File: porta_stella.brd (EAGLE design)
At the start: 220 x 100 mm, 80 parts, among them IC1 74LS00D, T1 2N3904, T2 PN3906, T3 PN3906, T4 PN3906, X1 SSW-112-02-G-Q

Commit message: Started work on controller daughterboard
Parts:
- removed C12: 1F, resistor:E3,5-8
- removed C13: 100nF, resistor:C0805
- removed ON/OFF: ON/OFF, special:EDG-01
- removed PAD1: AUD, wirepad:4,16O1,6
- removed PAD2: CVID, wirepad:4,16O1,6
- removed SV1: (no value), con-lstb:MA03-1
- removed USB1: ZX62-B-5PA, Seeed-Connector:MICRO-USB5+6P-SMD-0.65-AB
- added AUD: AUD, wirepad:2,54/1,1
- added C22: 10uf, adafruit:C0805
- added C5: 10uF, resistor:C1210
- added C6: 2.2uF, adafruit:C0805
- added C7: 0.1uF, adafruit:C0805
- added CHRG/LBO: ORANGE, piboy_new:ADAFRUIT_CHIPLED_0603
- added CN4: MicroUSB, microbuilder:4UCONN_20329
- added CVID: CVID, wirepad:2,54/1,1
- added DONE: GREEN, piboy_new:ADAFRUIT_CHIPLED_0603
- added GND_A: GND_A, wirepad:2,54/1,1
- added GND_V: GND_V, wirepad:2,54/1,1
- added L1: 6.8uH, microbuilder:INDUCTOR_5X5MM_TDK_VLC5045
- added LBO: RED, piboy_new:ADAFRUIT_CHIPLED_0603
- added ON: BLUE, piboy_new:ADAFRUIT_CHIPLED_0603
- added ON/OFF1: ON/OFF, special:EDG-01
- added R13, R36, R44, R45: 1K, adafruit:R0805
- added R37, R39: 200K, adafruit:R0805
- added R38, R41: 1.87M, adafruit:R0805
- added R40: 340K, adafruit:R0805
- added R42: 270K, adafruit:R0805
- added R43, R47: 100K, adafruit:R0805
- added R46: 1.0K, adafruit:R0805
- added SV2: (no value), con-lstb:MA10-1
- added T5: MMUN2133LT1G, piboy_new:TRANSISTOR_SC59-BEC
- added THERM: 15K, adafruit:R0805
- added U1: TPS61090RSAR, microbuilder:PVQFN-16
- added U2: MCP73871, microbuilder:QFN20_4MM
- C21: value 100nF -> 10uF; device resistor:C0805 -> resistor:C1210
- C9: value 68nF -> 10uF; device resistor:C0805 -> resistor:C1210
- S3, S4: device SparkFun-Switches:TACTILE_SWITCH_PTH_6.0MM_KIT -> SparkFun-Switches:TACTILE_SWITCH_SMD_6.0X3.5MM
- moved S4 134.0 mm to (162.1, 22.0), turned to 0 degrees
- moved C8 123.6 mm to (157.8, 9.83)
- moved C10 113.3 mm to (170.2, 39.2)
- moved C17 113.3 mm to (144.6, 85.6), turned to 0 degrees
- moved C9 111.8 mm to (14.0, -32.0), flipped to the top, turned to 0 degrees
- moved R34 111.5 mm to (141.1, 9.75), turned to 270 degrees
- moved C21 102.3 mm to (20.0, -32.0), flipped to the top, turned to 0 degrees
- moved JP1 102.1 mm to (168.1, 32.4), flipped to the bottom
- moved S3 97.5 mm to (136.5, 21.8), turned to 0 degrees
- moved C14 96.2 mm to (138.0, 59.5)
- moved LDIFF 87.2 mm to (125.0, 93.5), turned to 180 degrees
- moved PAUSE 86.4 mm to (171.0, 93.5), turned to 0 degrees
- moved COLOR 50.1 mm to (136.6, 74.6), turned to 180 degrees
- moved R33 26.6 mm to (170.1, 43.5), turned to 270 degrees
- moved C16 10.1 mm to (149.1, 36.3), turned to 90 degrees
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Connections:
- new net BOOST_ENABLE: ON/OFF1.1, R37.2, U1.11
- new net LBO: T5.B, U1.12
- new net N$10: L1.P$2, U1.3, U1.4
- new net N$12: R40.2, R41.1, U1.9
- new net N$22: LBO.A, R13.1
- new net N$37: R38.1, R39.2, U1.14
- new net N$41: R13.2, T5.C
- new net N$42: ON.A, R36.2
- new net N$43: R42.1, R43.1, U2.P$2
- new net N$44: R45.1, U2.P$7
- new net N$45: R44.1, U2.P$8
- new net N$46: R46.2, U2.P$13
- new net N$47: THERM.2, U2.P$5
- new net N$48: DONE.C, R45.2
- new net N$49: CHRG/LBO.C, R44.2
- new net N$50: R47.2, U2.P$12
- new net VBAT: C5.1, C7.1, L1.P$1, R37.1, R41.2, T5.E, U1.8, U2.P$1, U2.P$20
- new net VLIPO: C21.1, U2.P$14, U2.P$15, U2.P$16
- net +5V: now also C6.1, C9.1, R36.1, R38.2, SV3.2, U1.1, U1.15, U1.16; no longer C12.+, C13.1, ON/OFF.2
- net GND: now also C22.2, C5.2, C6.2, C7.2, CN4.BASE@1, CN4.BASE@2, CN4.D+, CN4.D-, CN4.GND, CN4.ID, CN4.SPRT@1, CN4.SPRT@2, CN4.SPRT@3, CN4.SPRT@4, GND_A.1, GND_V.1, LBO.C, ON.C, ON/OFF1.2, R39.1, R40.1, R43.2, R46.1, R47.1, S3.2, S4.2, SV2.1, THERM.1, U1.10, U1.13, U1.5, U1.6, U1.7, U1.P$18, U1.P$19, U1.P$20, U1.P$21, U1.P$22, U1.THERMAL, U2.P$10, U2.P$11, U2.P$21; no longer C12.-, C13.2, S3.3, S4.3, SV1.2, SV1.3, USB1.2, USB1.3, USB1.4, USB1.5, USB1.P1, USB1.P2, USB1.P3, USB1.P4, USB1.P5, USB1.P6
- net LFT_FIRE: now also SV2.4
- net LFT_JOY_DWN: now also SV2.9
- net LFT_JOY_LFT: now also SV2.8
- net LFT_JOY_RGT: now also SV2.7
- net LFT_JOY_UP: now also SV2.10
- net LFT_PADDLE_A: now also SV2.6
- net LFT_PADDLE_B: now also SV2.5; no longer C9.1
- net N$25: now also CVID.1; no longer PAD2.1
- net N$28: now also AUD.1; no longer PAD1.1
- net P_SW: now also SV2.3
- net VBUS: now also C22.1, CHRG/LBO.A, CN4.VBUS, DONE.A, R42.2, U2.P$17, U2.P$18, U2.P$19, U2.P$3, U2.P$4, U2.P$9; no longer ON/OFF.1, SV1.1, USB1.1
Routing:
- net D1: track 75.6 -> 68.8 mm
- net D8: track 134.6 -> 136.6 mm, vias 6 -> 5
- net A8: track 18.6 -> 19.9 mm
- net A5: track 50.9 -> 52.1 mm
- net A6: track 54.8 -> 56.1 mm
- net D7: track 129.7 -> 130.7 mm, vias 4 -> 3
- net A4: track 49.3 -> 50.2 mm
- net A3: track 48.0 -> 48.9 mm
- net D6: track 107.8 -> 108.6 mm
- net A11: track 25.4 -> 26.2 mm
- net A10: track 23.1 -> 23.7 mm
- net A9: track 57.9 -> 57.3 mm, vias 3 -> 2
- net A2: track 48.2 -> 48.8 mm
- removed copper zone on layer 1, net GND
- removed copper zone on layer 16, net GND
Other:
- board size 220 x 100 mm -> 52 x 99 mm
- board text removed: "+5V"
- board text removed: "A0"
- board text removed: "A1"
- board text removed: "A10"
- board text removed: "A11"
- board text removed: "A12"
- board text removed: "A2"
- board text removed: "A3"
- board text removed: "A4"
- board text removed: "A5"
- board text removed: "A6"
- board text removed: "A7"
- board text removed: "A8"
- board text removed: "A9"
- board text removed: "ADDRESS BUS"
- board text removed: "AU1"
- board text removed: "AU2"
- board text removed: "AUDIO"
- board text removed: "Atari Television Interface Adapter"
- board text removed: "B/W"
- board text removed: "BLK"
- board text removed: "BUTTONS"
- board text removed: "BW/ COLOR"
- board text removed: "CLK"
- board text removed: "COL"
- board text removed: "CS1"
- board text removed: "D1"
- board text removed: "D2"
- board text removed: "D3"
- board text removed: "D4"
- board text removed: "D5"
- board text removed: "D6"
- board text removed: "D7"
- board text removed: "D8"
- board text removed: "DATA BUS"
- board text removed: "DEL"
- board text removed: "DWN"
- board text removed: "GND"
- board text removed: "IRQ"
- board text removed: "LEFT DIFF."
- board text removed: "LEFT FIRE"
- board text removed: "LEFT JOYSTICK"
- board text removed: "LEFT PADDLE A"
- board text removed: "LEFT PADDLE B"
- board text removed: "LEFT PLAYER"
- board text removed: "LFT"
- board text removed: "LM0"
- board text removed: "LM1"
- board text removed: "LM2"
- board text removed: "MOS Technologies 6507 Microprocessor"
- board text removed: "MOS Technologies 6532 RIOT Chip"
- board text removed: "PADDLES"
- board text removed: "PB2"
- board text removed: "PB4"
- board text removed: "PB5"
- board text removed: "PHI0"
- board text removed: "PHI2"
- board text removed: "R/W"
- board text removed: "RDY"
- board text removed: "RES"
- board text removed: "RESET"
- board text removed: "RGT"
- board text removed: "RIGHT DIFF."
- board text removed: "RIGHT FIRE"
- board text removed: "RIGHT JOYSTICK"
- board text removed: "RIGHT PADDLE A"
- board text removed: "RIGHT PADDLE B"
- board text removed: "RIGHT PLAYER"
- board text removed: "SELECT"
- board text removed: "START"
- board text removed: "SWITCHES"
- board text removed: "SYNC"
- board text removed: "This chip serves two functions; It holds the system's 128 bytes of RAM and gives the CPU more I/O so it can connect with all the controllers and difficulty switches."
- board text removed: "This chip was custom manufactured by Atari and is responsible for drawing everything on the screen, producing sound, and reading some controller input. It's considered by many to be the soul of the system"
- board text removed: "This was a cost reduced version of the very popular 6502 processor"
- board text removed: "UP"
- board text removed: "Use at least 500mA Supply"
- board text removed: "VIDEO"

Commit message: reworked the shape
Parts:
- removed SV2, SV3: (no value), con-lstb:MA10-1
- added J1: PJ-393, Seeed-Connector:AUDIO8P-SMD-3.5-14.5X6.1X4.0MM
- moved PAUSE 176.9 mm to (4.00, 35.0), turned to 180 degrees
- moved R40 165.2 mm to (133.1, 53.3), flipped to the bottom, turned to 180 degrees
- moved R36 161.6 mm to (132.9, 41.3), flipped to the bottom, turned to 180 degrees
- moved R38 161.4 mm to (127.4, 60.3), flipped to the bottom, turned to 90 degrees
- moved R41 159.0 mm to (133.8, 57.2), flipped to the bottom, turned to 90 degrees
- moved S4 157.3 mm to (6.00, 42.0), turned to 180 degrees
- moved S2 156.2 mm to (7.00, 24.8), turned to 90 degrees
- moved U1 154.5 mm to (128.6, 55.5), flipped to the bottom, turned to 270 degrees
- moved R44 153.0 mm to (128.8, 39.3), flipped to the bottom
- moved R45 152.3 mm to (132.9, 39.3), flipped to the bottom, turned to 180 degrees
- moved C6 152.2 mm to (129.5, 60.3), flipped to the bottom, turned to 270 degrees
- moved C9 148.1 mm to (126.9, 63.8), flipped to the bottom
- moved C5 146.4 mm to (129.1, 50.2), flipped to the bottom, turned to 270 degrees
- moved C17 143.8 mm to (15.4, 22.5), turned to 270 degrees
- moved T5 141.0 mm to (129.1, 44.2), flipped to the bottom, turned to 180 degrees
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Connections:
- net +5V: no longer SV3.2
- net GND: no longer SV2.1, SV3.1
- net LFT_FIRE: no longer SV2.4, SV3.4
- net LFT_JOY_DWN: no longer SV2.9, SV3.9
- net LFT_JOY_LFT: no longer SV2.8, SV3.8
- net LFT_JOY_RGT: no longer SV2.7, SV3.7
- net LFT_JOY_UP: no longer SV2.10, SV3.10
- net LFT_PADDLE_A: no longer SV2.6, SV3.6
- net LFT_PADDLE_B: no longer SV2.5, SV3.5
- net P_SW: no longer SV2.3, SV3.3
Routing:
- net D8: track 136.6 -> 69.5 mm, vias 5 -> 4
- net D7: track 130.7 -> 69.9 mm, vias 3 -> 2
- net A9: track 57.3 -> 0.00 mm, vias 2 -> 0
- net D6: track 108.6 -> 52.4 mm, vias 4 -> 2
- net A6: track 56.1 -> 3.52 mm, vias 1 -> 0
- net D5: track 94.9 -> 43.8 mm, vias 4 -> 2
- net D4: track 89.2 -> 41.2 mm
- net D3: track 73.9 -> 33.8 mm
- net D2: track 70.0 -> 31.7 mm
- net D1: track 68.8 -> 31.7 mm
- net A5: track 52.1 -> 22.2 mm, vias 1 -> 0
- net A4: track 50.2 -> 22.8 mm, vias 1 -> 0
- net A11: track 26.2 -> 0.00 mm, vias 1 -> 0
- net A3: track 48.9 -> 23.5 mm, vias 1 -> 0
- net A12: track 59.1 -> 34.5 mm
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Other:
- board size 52 x 99 mm -> 98 x 62 mm
- board text added: "QUARTER DOLLAR"
- board text added: "UNITED STATES OF AMERICA"

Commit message: more trace work
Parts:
- moved C6 60.1 mm to (76.2, 32.4), turned to 0 degrees
- moved C9 58.7 mm to (75.7, 34.9)
- moved L1 58.6 mm to (74.0, 37.5), turned to 0 degrees
- moved R40 58.3 mm to (75.7, 42.8), turned to 270 degrees
- moved R41 57.1 mm to (78.8, 41.9), turned to 180 degrees
- moved R38 54.5 mm to (81.2, 31.4), turned to 270 degrees
- moved R39 52.0 mm to (80.2, 34.4), turned to 180 degrees
- moved U1 51.8 mm to (79.8, 38.2), turned to 180 degrees
- moved T5 46.5 mm to (83.9, 33.4)
- moved C5 45.3 mm to (85.2, 39.0), turned to 180 degrees
- moved R37 43.9 mm to (84.7, 36.4), turned to 0 degrees
- moved ON 43.6 mm to (90.9, 29.9), turned to 270 degrees
- moved R36 43.5 mm to (90.9, 29.9), turned to 0 degrees
- moved DONE 42.8 mm to (90.8, 31.9), turned to 90 degrees
- moved R45 42.6 mm to (90.9, 31.9), turned to 0 degrees
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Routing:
- net +5V: track 0.00 -> 128.7 mm, vias 0 -> 7
- net P_SW: track 0.00 -> 30.0 mm, vias 0 -> 2
- net N$40: track 0.00 -> 28.8 mm, vias 0 -> 2
- net N$45: track 0.00 -> 28.6 mm, vias 0 -> 2
- net VBAT: track 0.00 -> 27.2 mm, vias 0 -> 1
- net VBUS: track 0.00 -> 26.3 mm, vias 0 -> 3
- net N$28: track 0.00 -> 24.5 mm, vias 0 -> 1
- net N$44: track 0.00 -> 23.8 mm, vias 0 -> 2
- net LFT_PADDLE_A: track 0.00 -> 22.6 mm
- net N$32: track 0.00 -> 22.0 mm, vias 0 -> 2
- net CPU_RDY: track 0.00 -> 21.6 mm, vias 0 -> 2
- net N$17: track 0.00 -> 20.9 mm, vias 0 -> 1
- net TIA_RDY: track 0.00 -> 17.9 mm, vias 0 -> 1
- net N$5: track 0.00 -> 17.0 mm
- net N$4: track 0.00 -> 16.5 mm, vias 0 -> 2
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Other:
- outline, holes or cut-outs redrawn

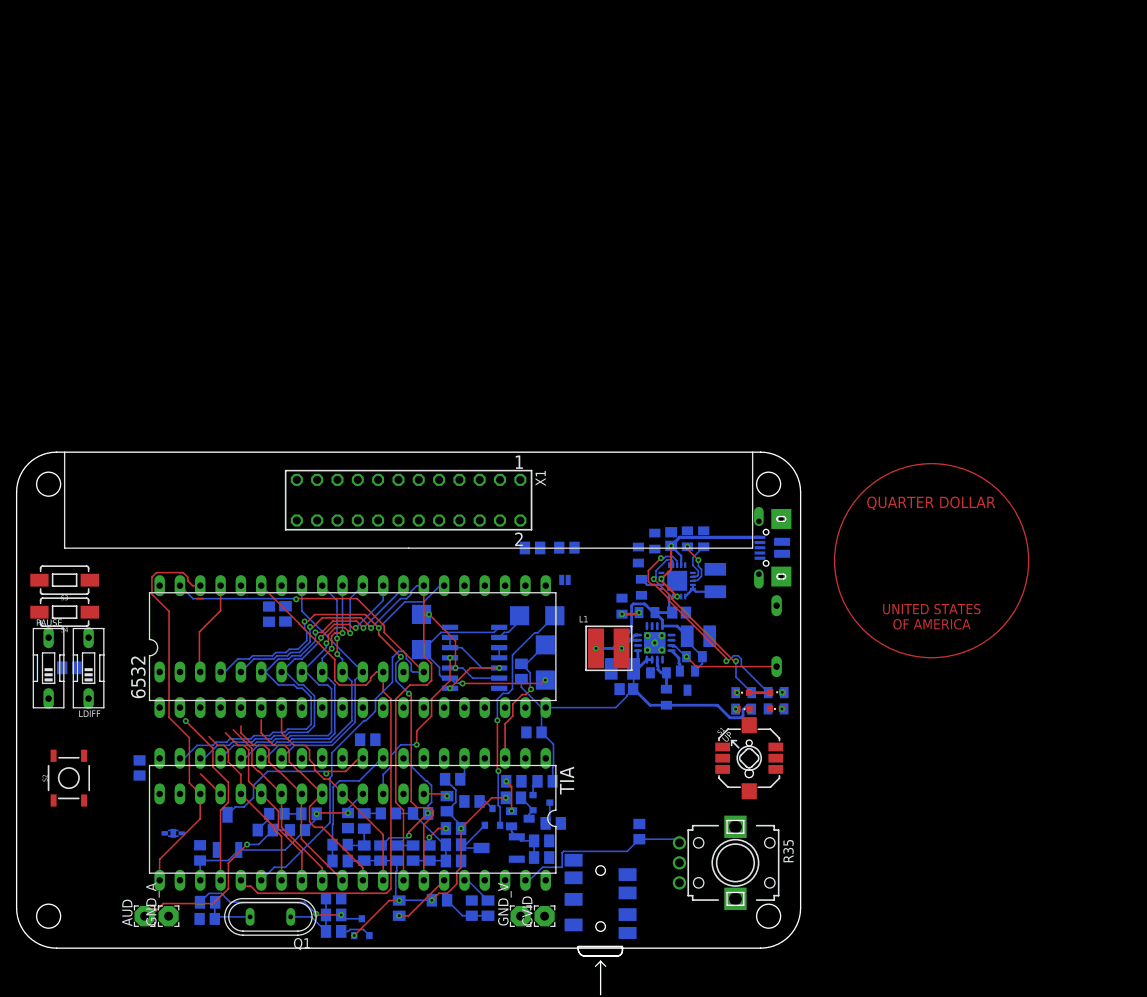
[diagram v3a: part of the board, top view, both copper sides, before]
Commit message: included measurements of the screen
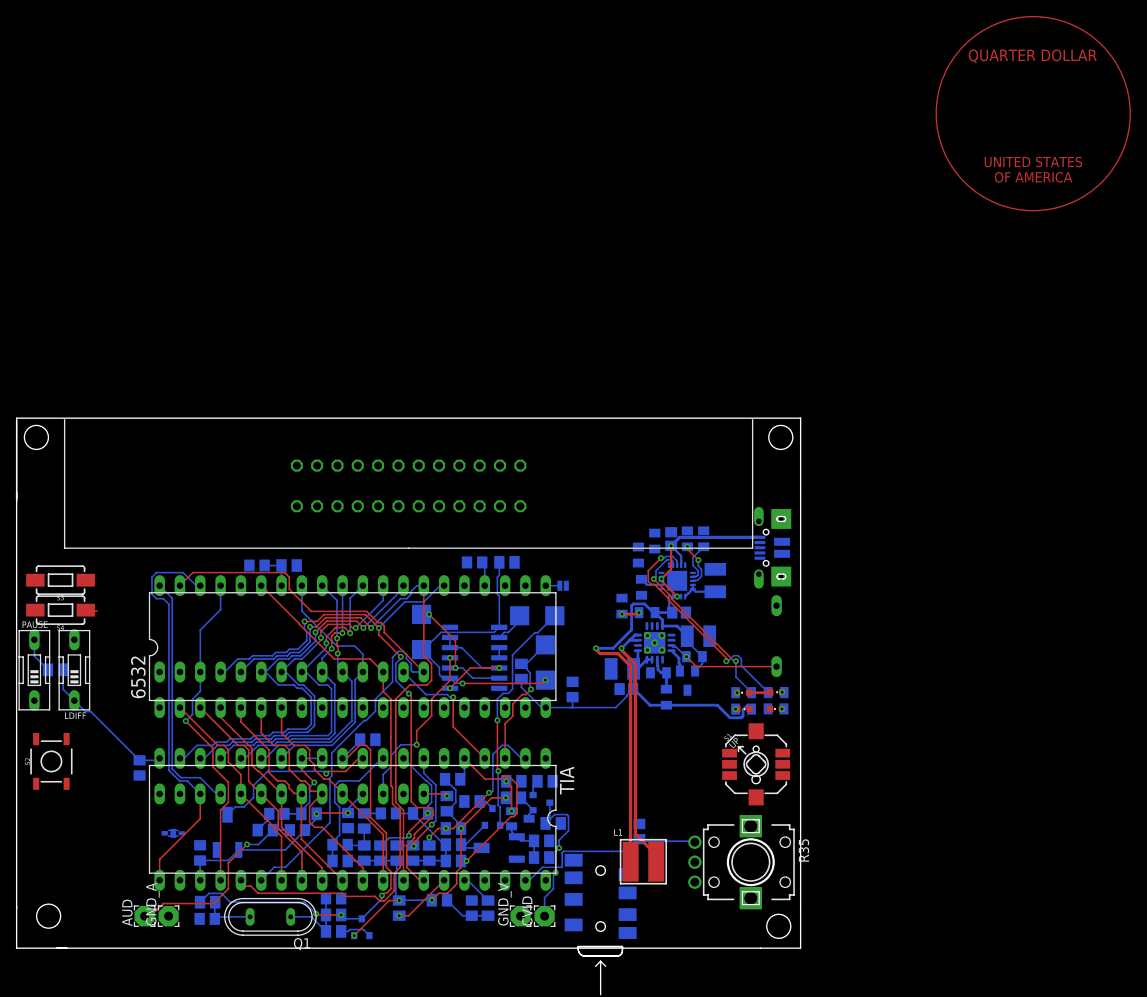
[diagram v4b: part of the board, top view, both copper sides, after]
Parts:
- moved L1 27.0 mm to (78.3, 10.8)
- moved C10 11.7 mm to (57.3, 48.2), turned to 0 degrees
- moved C16 7.21 mm to (69.5, 32.3), turned to 90 degrees
- moved C18 6.25 mm to (30.0, 47.8), turned to 0 degrees
- moved R27 6.06 mm to (34.1, 47.8), turned to 0 degrees
- moved R33 3.67 mm to (61.3, 48.2)
- moved S2 3.02 mm to (4.35, 23.3)
- moved R35 1.93 mm to (91.8, 10.7)
- moved PAUSE 1.80 mm to (2.22, 34.7)
- moved LDIFF 1.80 mm to (7.22, 34.7)
- moved R34 1.80 mm to (4.87, 34.8)
- moved X1 1.78 mm to (49.0, 57.8), flipped to the bottom
- moved S1 1.15 mm to (92.4, 23.0)
- moved JP1 0.75 mm to (68.3, 45.3), turned to 180 degrees
- moved S4 0.57 mm to (5.49, 42.3)
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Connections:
- net LFT_FIRE: now also S2.1
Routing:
- net N$32: track 22.0 -> 53.5 mm, vias 2 -> 3
- net VBAT: track 27.2 -> 56.9 mm
- net N$10: track 3.75 -> 32.2 mm
- net A6: track 3.52 -> 30.9 mm
- net N$2: track 2.83 -> 24.2 mm, vias 0 -> 1
- net N$1: track 3.54 -> 21.1 mm, vias 2 -> 3
- net N$25: track 2.81 -> 20.0 mm, vias 0 -> 2
- net PHI_0: track 0.00 -> 16.8 mm, vias 0 -> 1
- net N$3: track 2.03 -> 15.0 mm, vias 0 -> 2
- net N$27: track 2.11 -> 12.9 mm, vias 0 -> 1
- net +5V: track 128.7 -> 138.4 mm
- net N$40: track 28.8 -> 37.1 mm
- net A12: track 34.5 -> 41.3 mm
- net A5: track 22.2 -> 27.3 mm
- net N$29: track 0.00 -> 4.63 mm
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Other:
- board size 98 x 62 mm -> 98 x 66.2 mm
- board text added: "screen"

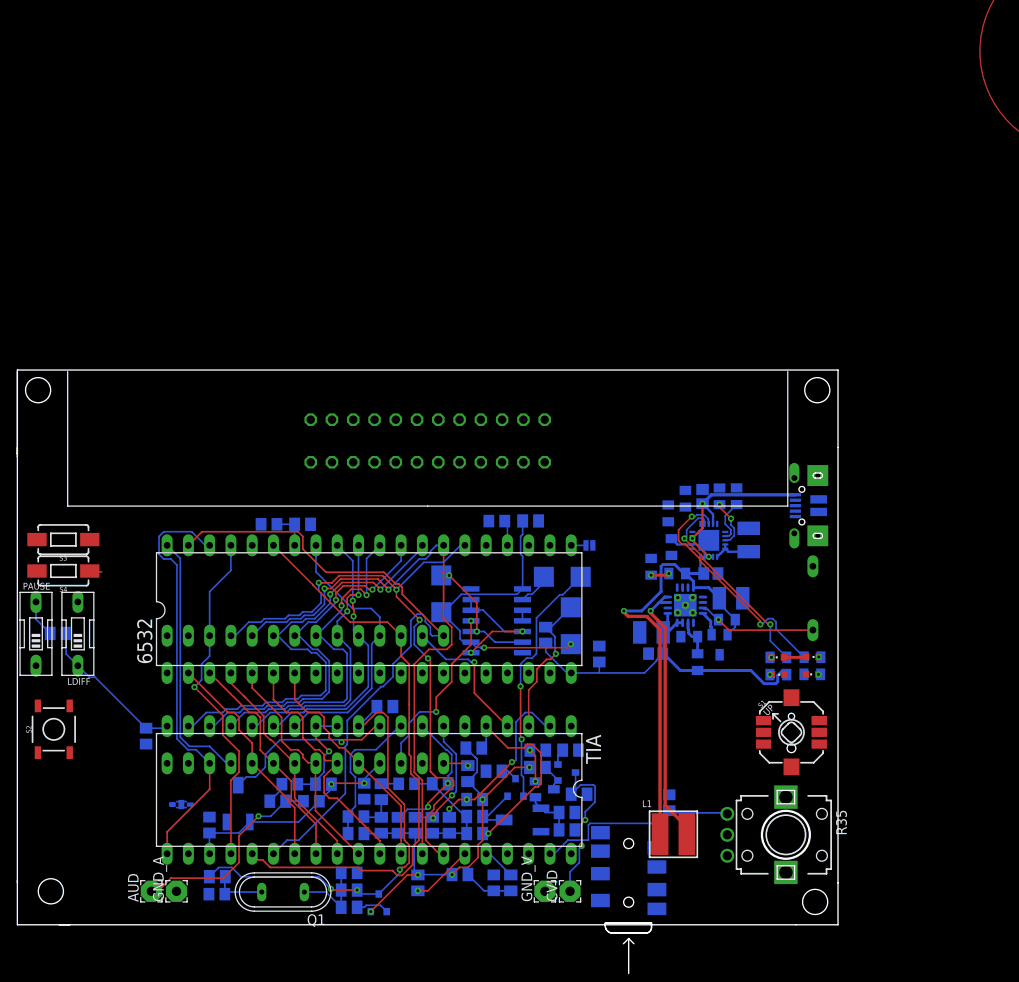
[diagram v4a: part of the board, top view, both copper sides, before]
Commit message: resized again to make more room for the joystick
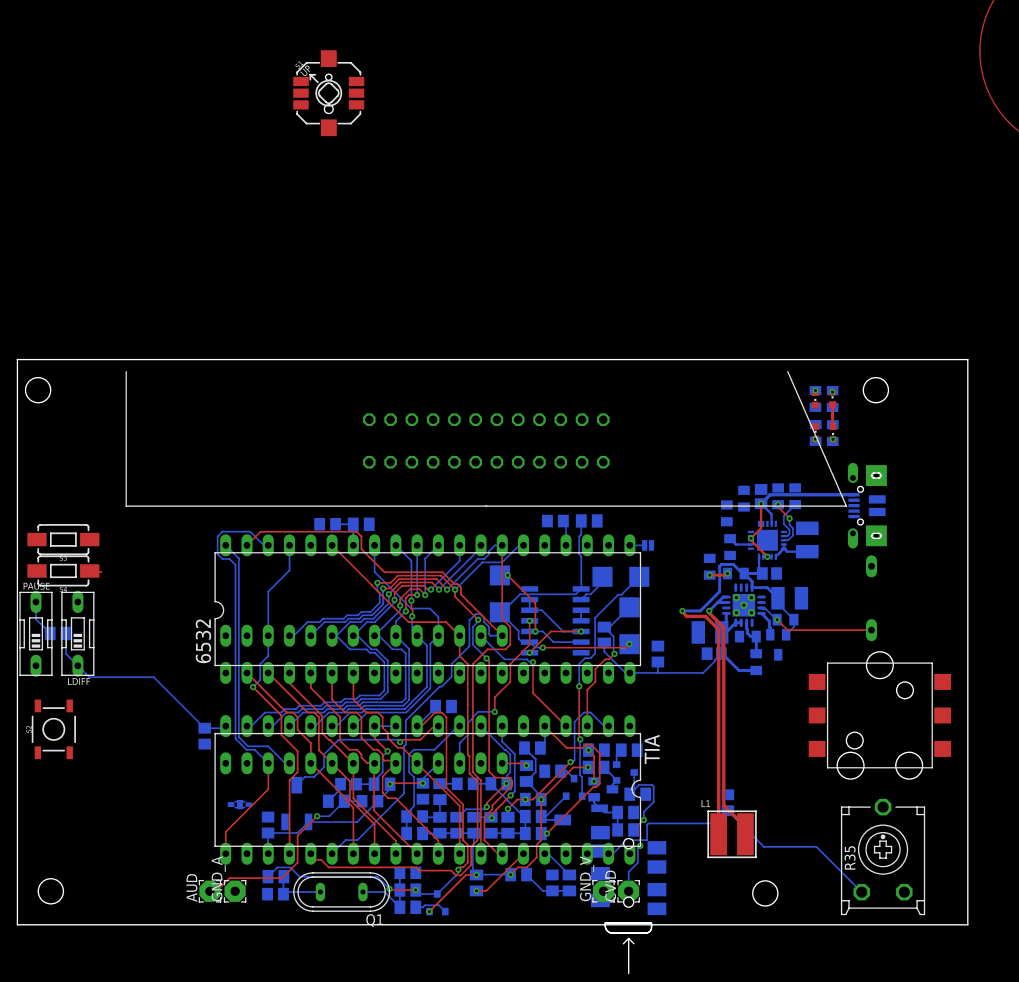
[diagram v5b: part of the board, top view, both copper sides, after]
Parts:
- added U$5: JS5208, tiny_stella:JS5208_PKG
- R35: value EVUF2A -> (none); device pot:EVUF -> pot:ECP10S
- moved S1 94.2 mm to (37.2, 99.3)
- moved ON 33.2 mm to (95.3, 62.8), turned to 180 degrees
- moved R36 33.2 mm to (95.3, 62.8), turned to 90 degrees
- moved DONE 31.6 mm to (97.4, 62.9), turned to 0 degrees
- moved R45 31.5 mm to (97.4, 62.8), turned to 90 degrees
- moved LBO 28.9 mm to (95.3, 58.8), turned to 0 degrees
- moved R13 28.8 mm to (95.3, 58.7), turned to 90 degrees
- moved R44 26.9 mm to (97.4, 58.7), turned to 270 degrees
- moved CHRG/LBO 26.8 mm to (97.4, 58.7), turned to 180 degrees
- moved R35 11.7 mm to (103.4, 8.97), turned to 0 degrees
- moved R16 7.00 mm to (65.9, 5.00)
- moved T1 7.00 mm to (70.0, 16.2)
- moved Q1 7.00 mm to (38.7, 3.91)
- moved 6507 7.00 mm to (41.4, 26.9)
- moved 6532 7.00 mm to (49.0, 37.7)
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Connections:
- net GND: now also R35.S; no longer R35.2
- net LFT_PADDLE_A: now also R35.A; no longer R35.1
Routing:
- net N$45: track 28.6 -> 0.00 mm, vias 2 -> 0
- net N$44: track 23.8 -> 0.00 mm, vias 2 -> 0
- net LFT_PADDLE_A: track 24.5 -> 37.5 mm
- net +5V: track 138.4 -> 132.8 mm
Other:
- board size 98 x 66.2 mm -> 113.5 x 67.5 mm
